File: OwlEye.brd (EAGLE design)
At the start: 160 x 100 mm, 40 parts

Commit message: Starting to route using the second layer and vias
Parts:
- moved ONES:C6 223.6 mm to (31.0, 87.6)
- moved ONES:C5 221.7 mm to (22.9, 85.9)
- moved ONES:C2 207.4 mm to (30.7, 70.6)
- moved ONES:C1 205.6 mm to (23.4, 69.1)
- moved ONES:C4 205.0 mm to (46.2, 67.3)
- moved ONES:C3 202.8 mm to (38.6, 65.5)
- moved ONES:C10 191.3 mm to (17.5, 54.9)
- moved ONES:C7 191.3 mm to (45.5, 54.9)
- moved ONES:C8 191.3 mm to (17.5, 51.1)
- moved ONES:C9 191.3 mm to (21.3, 51.1)
- moved TENS:C8 139.4 mm to (72.4, 87.6), turned to 180 degrees
- moved TENS:C7 124.5 mm to (79.0, 69.1)
- moved TENS:C6 118.3 mm to (71.4, 70.9)
- moved TENS:C5 106.5 mm to (63.8, 65.5)
- moved TENS:C4 100.6 mm to (56.1, 67.3)
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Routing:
- net GND: track 60.9 -> 192.9 mm
- net VCC: track 66.4 -> 167.1 mm
- net ONES:N$7: track 0.00 -> 22.5 mm, vias 0 -> 2
- net ONES:N$12: track 0.00 -> 21.6 mm, vias 0 -> 2
- net N$1: track 0.00 -> 16.4 mm, vias 0 -> 2
- net ONES:N$1: track 0.00 -> 15.8 mm, vias 0 -> 2
- net TENS:N$13: track 0.00 -> 14.8 mm, vias 0 -> 2
- net TENS:N$6: track 0.00 -> 14.2 mm, vias 0 -> 2
- net TENS:N$1: track 0.00 -> 13.3 mm
- net TENS:N$5: track 0.00 -> 13.2 mm
- net ONES:N$15: track 0.00 -> 4.85 mm
- net ONES:N$10: track 0.00 -> 4.81 mm
- net ONES:N$6: track 0.00 -> 4.77 mm
- net ONES:N$5: track 0.00 -> 4.74 mm
- net ONES:N$13: track 0.00 -> 4.70 mm
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
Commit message: After smashing and text adjustment
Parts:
- moved TENS:C10 11.8 mm to (42.2, 54.9)
- moved ONES:C8 5.21 mm to (21.1, 54.9)
- moved ONES:C9 4.88 mm to (24.4, 54.9)
- moved TENS:C2 0.51 mm to (50.8, 78.7)
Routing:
- net TENS:N$13: track 14.8 -> 0.00 mm, vias 2 -> 0

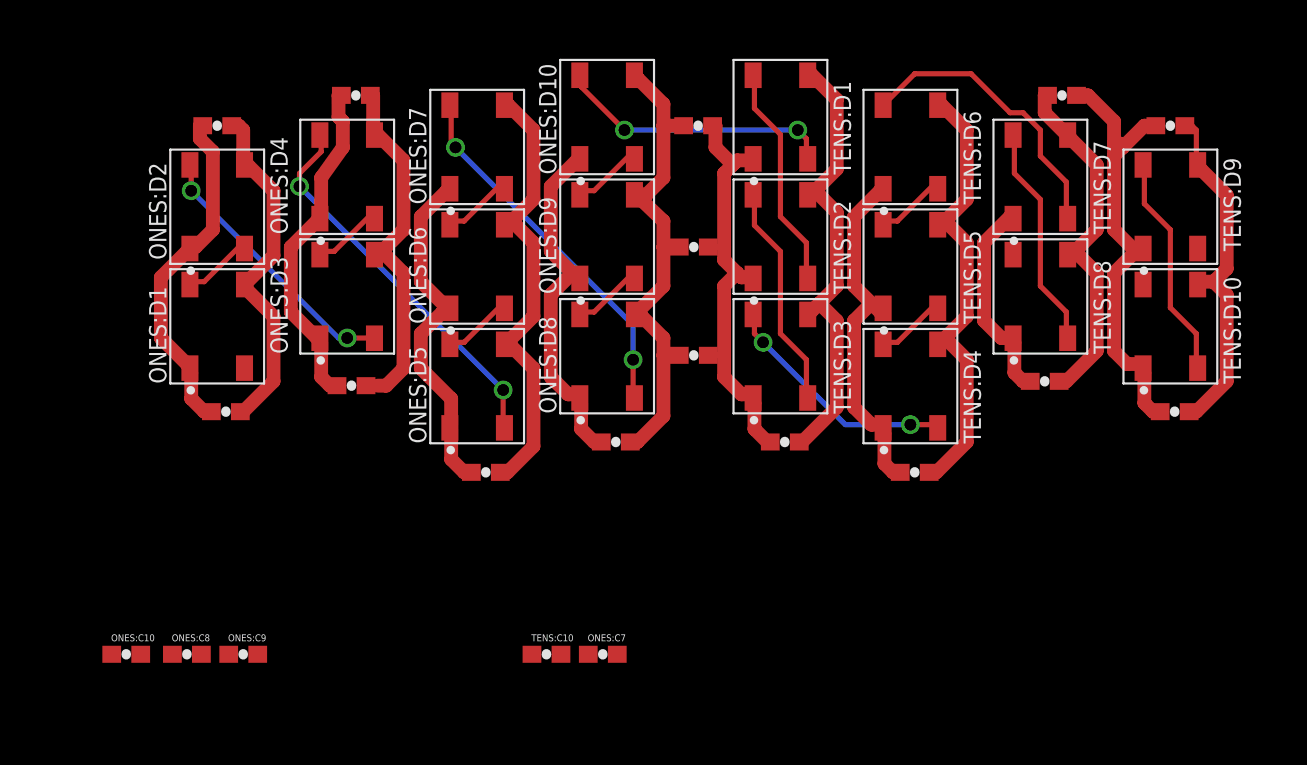
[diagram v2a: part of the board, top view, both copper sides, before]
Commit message: Removed the extra caps
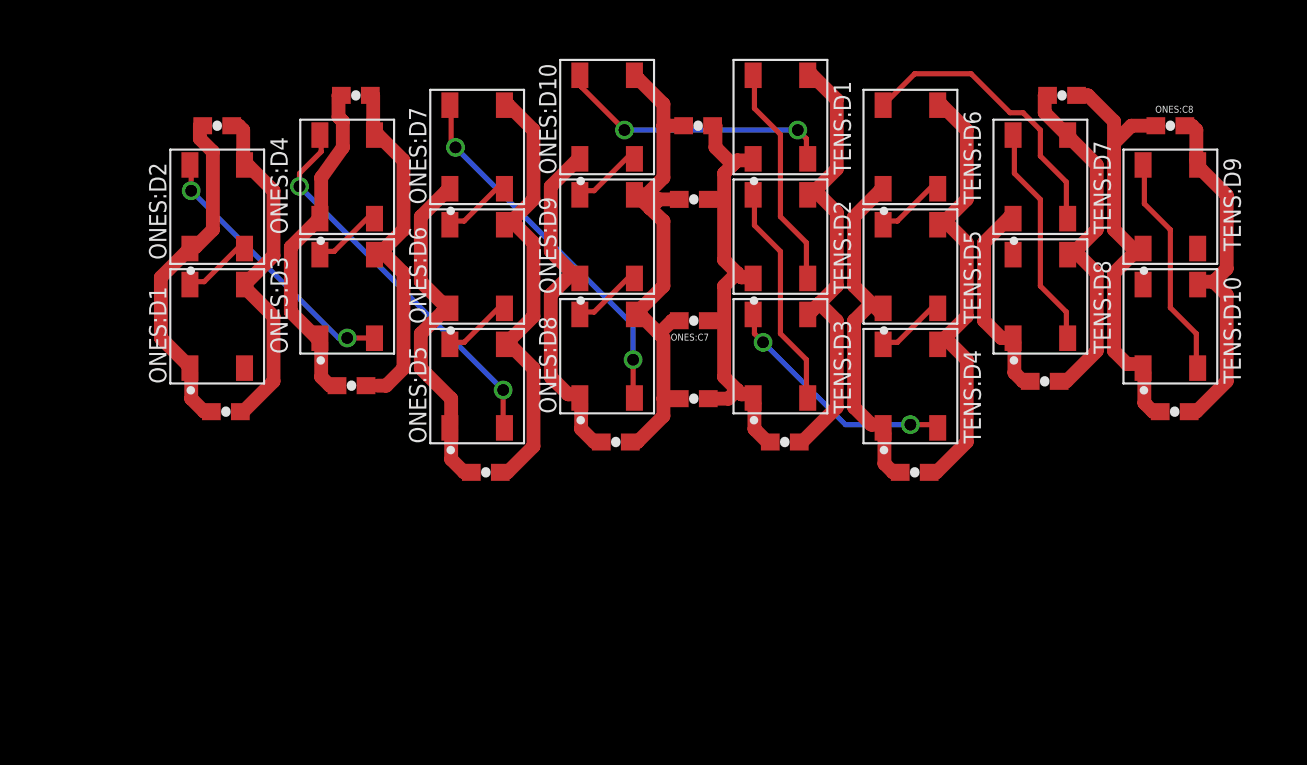
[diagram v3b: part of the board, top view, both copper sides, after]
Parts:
- removed ONES:C10, ONES:C9, TENS:C10, TENS:C9: 0.1uF, SparkFun-Capacitors:0603-CAP
- moved ONES:C8 65.5 mm to (78.7, 85.9)
- moved ONES:C7 20.3 mm to (50.8, 74.4), turned to 180 degrees
- moved TENS:C2 2.79 mm to (50.8, 81.5)
- moved TENS:C3 2.54 mm to (50.8, 69.8)
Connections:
- net GND: no longer ONES:C10.2, ONES:C9.2, TENS:C10.2, TENS:C9.2
- net VCC: no longer ONES:C10.1, ONES:C9.1, TENS:C10.1, TENS:C9.1
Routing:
- net GND: track 192.9 -> 195.4 mm
- net VCC: track 167.1 -> 168.1 mm
